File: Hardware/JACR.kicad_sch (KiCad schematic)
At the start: 37 parts, among them J1 Barrel_Jack_Switch, J2 JACR CARTRIDGE SLOT, J3 EXP1, J4 EXP2, Q1 BSS138, Q2 BSS138, SW1 SW_SPST, U1 TPS563200, U2 TPS563200, U4 DS3231MZ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

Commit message: Wrong Resistor values for the power regulator circuit
Not sure where I got the old values but rereading the data sheet and testing is key to not overvolt anything
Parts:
- J2, SW1, U5: now left out of the parts list
- R1: value 73.2kΩ -> 54.9kΩ
- R3: value 45.3kΩ -> 33.2kΩ
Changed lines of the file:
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@@
 		(unit 1)
 		(exclude_from_sim no)
-		(in_bom yes)
+		(in_bom no)
 		(on_board yes)
 		(dnp no)
@@
 		(unit 1)
 		(exclude_from_sim no)
-		(in_bom yes)
+		(in_bom no)
 		(on_board yes)
 		(dnp no)
@@
 		(unit 1)
 		(exclude_from_sim no)
-		(in_bom yes)
+		(in_bom no)
 		(on_board yes)
 		(dnp no)
@@
 			)
 		)
-		(property "Value" "45.3kΩ"
+		(property "Value" "33.2kΩ"
 			(at 151.13 35.5599 0)
 			(effects
@@
 			)
 		)
-		(property "Value" "73.2kΩ"
+		(property "Value" "54.9kΩ"
 			(at 88.9 26.6699 0)
 			(effects

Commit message: Modified power circuitry
Changed inductor to a more readily available part
Simplified 3.3V rail to linear regulator part
After some testing, reduced fuse value, the whole unit barely hits 1 amp, might be higher during dumping
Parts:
- removed C5: 47µF, Capacitor_SMD:C_0603_1608Metric, symbol Device:C_Small
- removed C6: 47µF, Capacitor_SMD:C_0603_1608Metric_Pad1.08x0.95mm_HandSolder, symbol Device:C_Small
- removed L2: 3.3µH, Generic:mps_mag_4600_smt_a, symbol Device:L_Small
- removed R3: 33.2kΩ, Resistor_SMD:R_0603_1608Metric_Pad0.98x0.95mm_HandSolder, symbol Device:R_Small_US
- removed R4: 10kΩ, Resistor_SMD:R_0603_1608Metric_Pad0.98x0.95mm_HandSolder, symbol Device:R_Small_US
- removed U2: TPS563200, Package_TO_SOT_SMD:SOT-23-6, symbol Regulator_Switching:TPS563200
- added C3: 47µF, Capacitor_SMD:C_0603_1608Metric_Pad1.08x0.95mm_HandSolder, symbol Device:C_Small
- added U2: LD1117S33, Package_TO_SOT_SMD:SOT-223-3_TabPin2, symbol Regulator_Linear:LD1117S33TR_SOT223
- C4: renamed from C2; value 10µF -> 0.1µF
- C5: renamed from C4; value 0.1µF -> 10µF
- F1: value 2.5A -> 1A
- L1: footprint Generic:mps_mag_4600_smt_a -> Inductor_SMD:L_APV_ANR5040; Part 46472C -> NR5040
- renumbered C3 to C2
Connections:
- net +3V3: now also C5.1, U2.2 (VO)
- net +5V: now also C4.1, C3.1, U2.3 (VI)
- net GND: now also C5.2, C3.2, U2.1 (GND)
- net VCC: no longer C4.1
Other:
- moved on the sheet: C4, C5

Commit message: Modified Clock Gnerator/RTC Circuit
I believe putting the RTC I2C lines behind the transistors and pullups is causing problems with it not registering as present all the time. It may also be interfering with the Clock Generator.
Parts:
- U1: value TPS563200 -> TPS562200
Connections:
- net +3V3: no longer C10.1, U4.2 (VCC)
- net +5V: now also C10.1, U4.2 (VCC)
- net D20: now also U4.7 (SDA)
- net D21: now also U4.8 (SCL)
- net SCL: no longer U4.8 (SCL)
- net SDA: no longer U4.7 (SDA)
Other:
- note added: "Real Time Clock"
- moved on the sheet: C10, C7, C8, C9, Q1, Q2, R5, R6, R7, R8, RTCBATT1, U4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

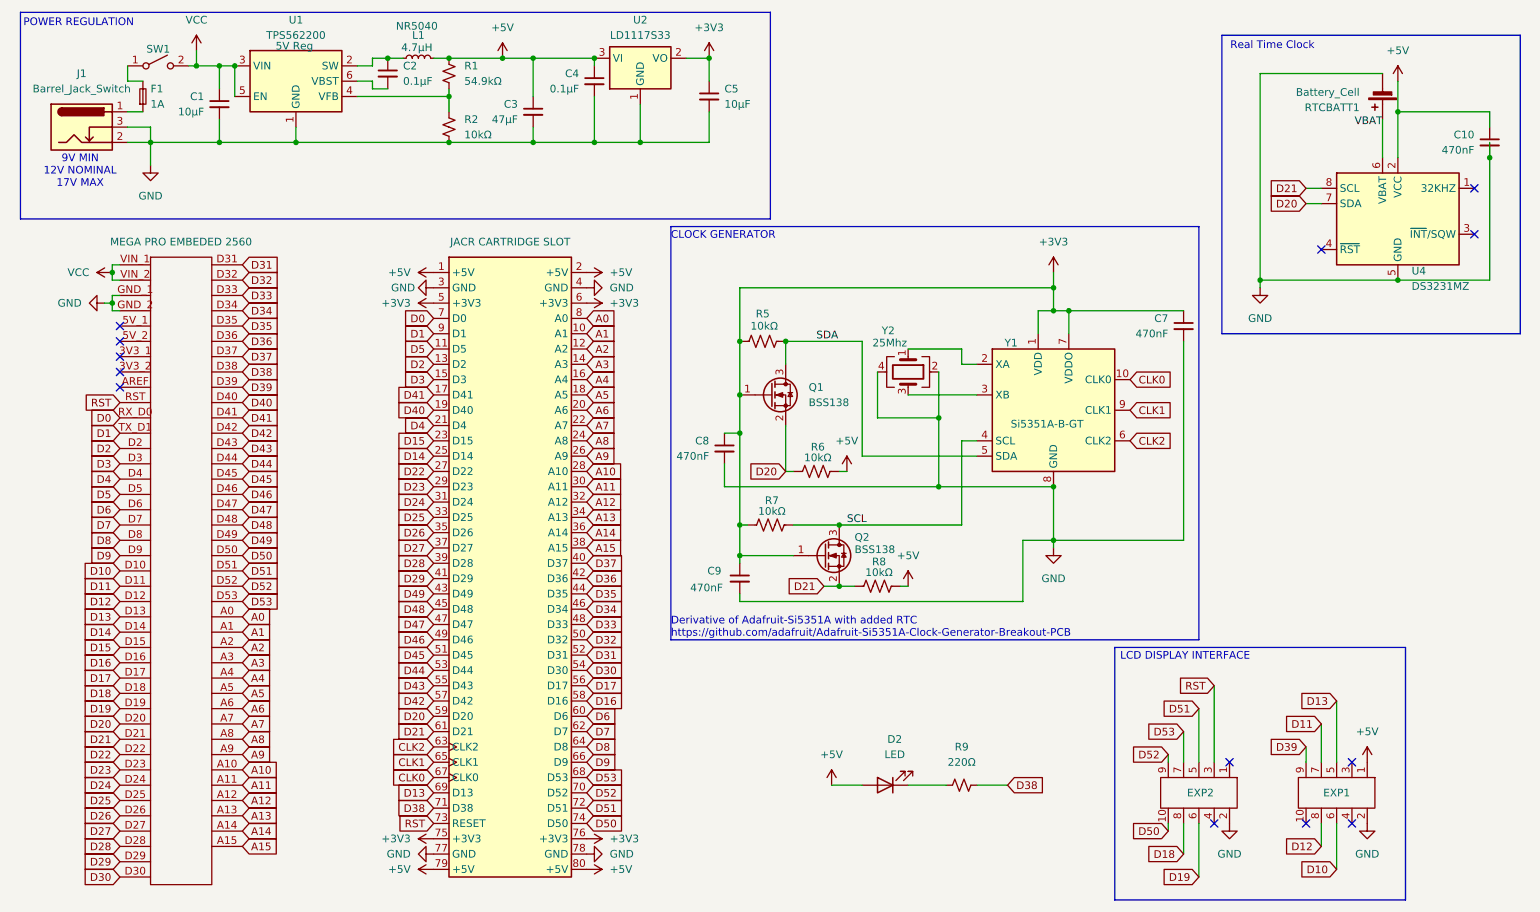
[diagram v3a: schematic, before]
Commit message: Corrected Source and Drain inputs on BSS138 in clock generator circuit
It would seem I have the 3V and 5V flipped and may have been the cause of my clock generator appearing to not work
also made adjustments to some traces
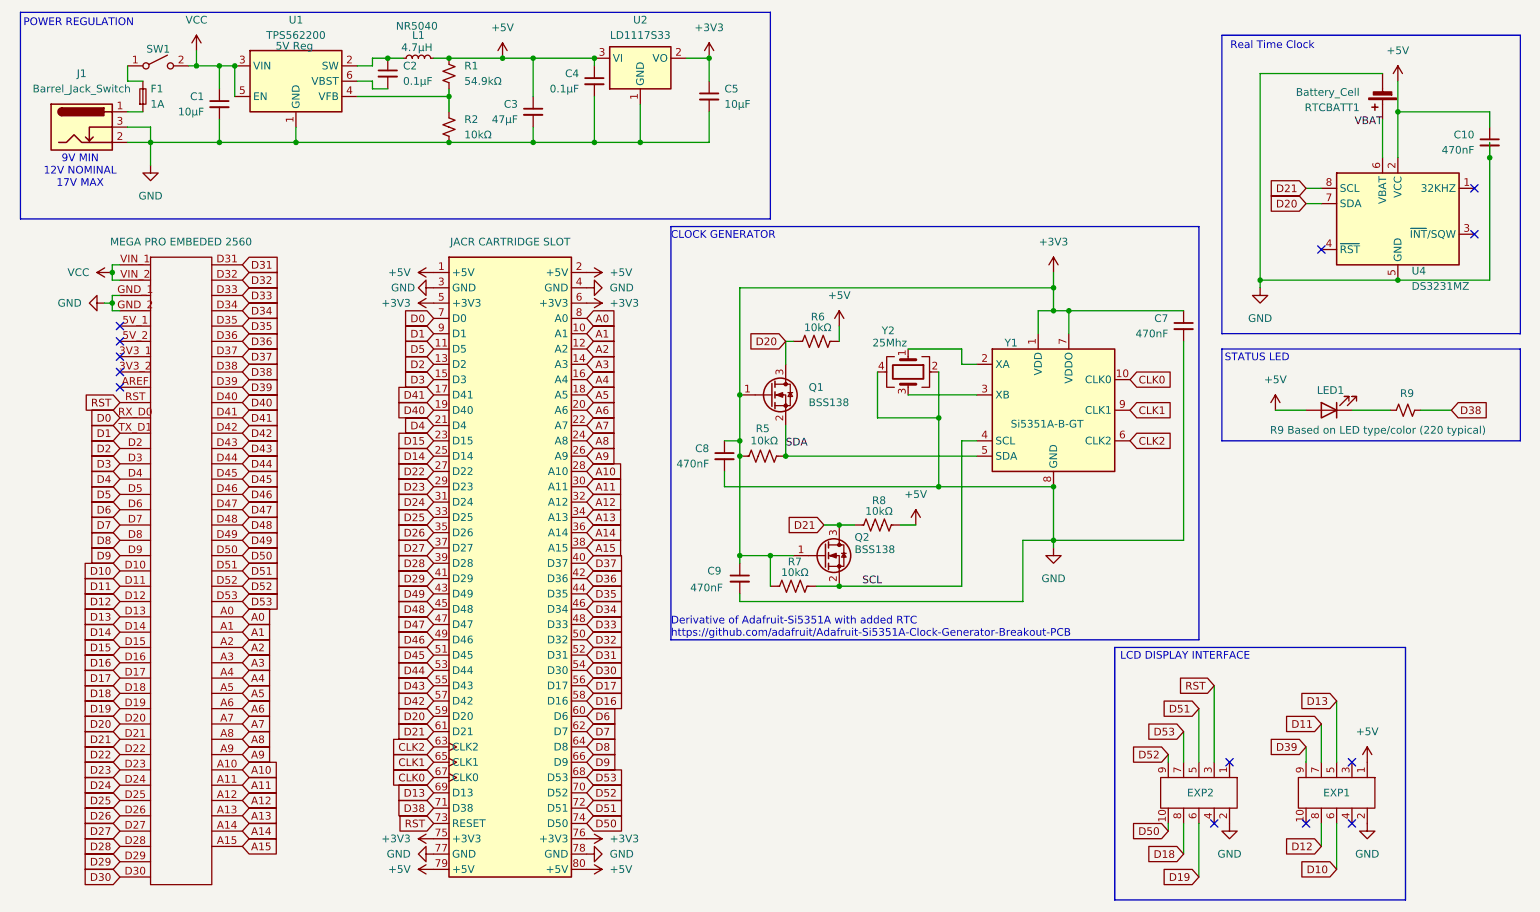
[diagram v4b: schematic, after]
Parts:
- R9: value 220Ω -> R9 Based on LED type/color (220 typical)
- renumbered D2 to LED1
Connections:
- net D20: now also Q1.3 (D); no longer Q1.2 (S)
- net D21: now also Q2.3 (D); no longer Q2.2 (S)
- net SCL: now also Q2.2 (S); no longer Q2.3 (D)
- net SDA: now also Q1.2 (S); no longer Q1.3 (D)
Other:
- note added: "STATUS LED"
- moved on the sheet: C8, LED1, R5, R6, R7, R8, R9
